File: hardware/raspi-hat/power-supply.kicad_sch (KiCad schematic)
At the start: 5 parts, among them J3 ATX-20, J4 Raspberry_Pi_4

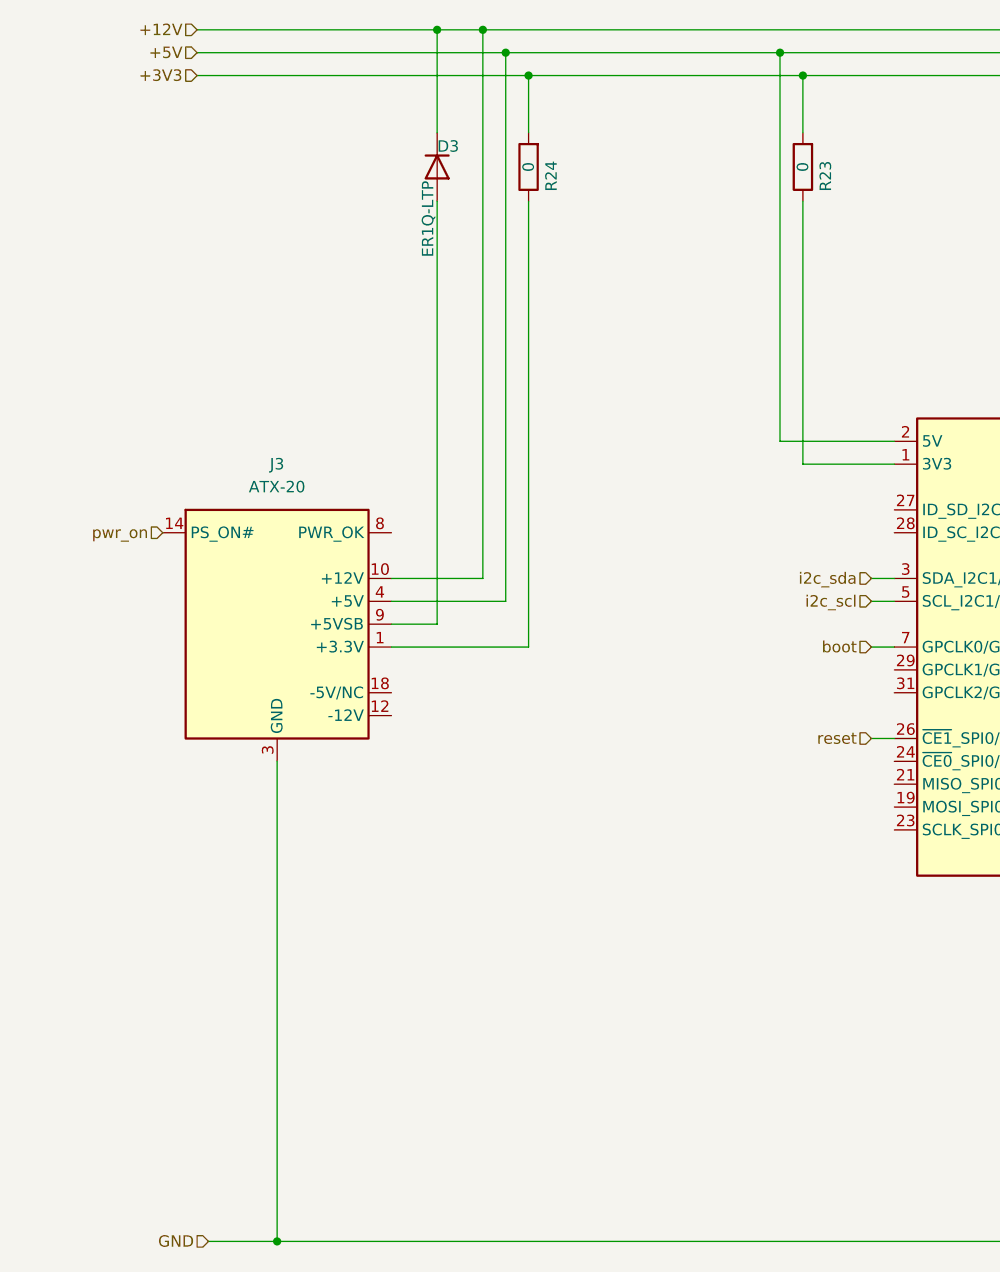
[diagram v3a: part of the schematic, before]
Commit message: added more parts
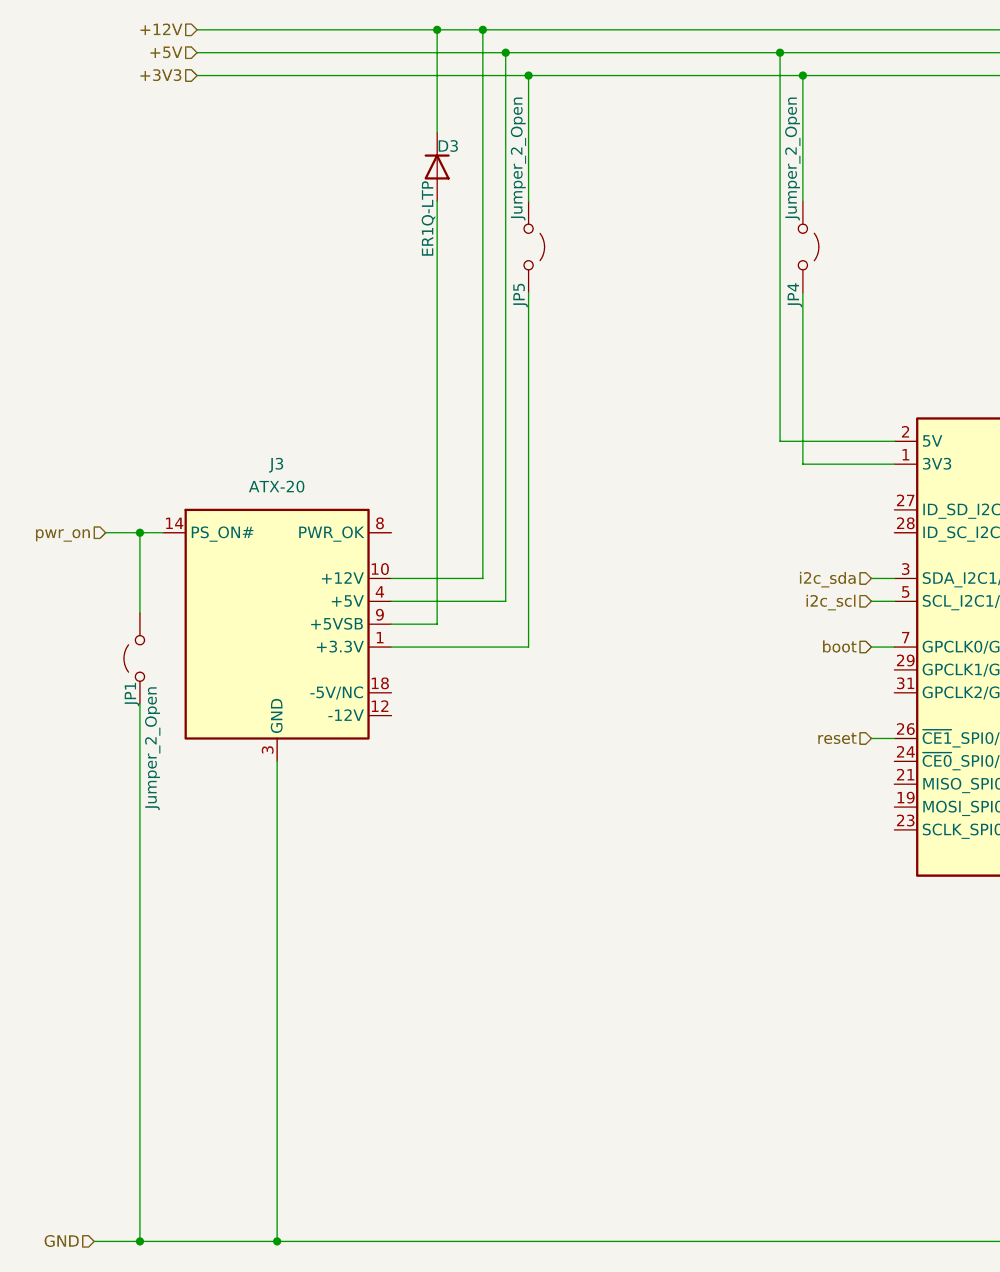
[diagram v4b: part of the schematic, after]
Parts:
- removed R23, R24: 0, Resistor_SMD:R_0603_1608Metric, symbol Device:R
- added JP1, JP4, JP5: Jumper_2_Open, Jumper:SolderJumper-2_P1.3mm_Open_TrianglePad1.0x1.5mm, symbol Jumper:Jumper_2_Open
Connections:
- net +3V3: now also JP4.1 (A), JP5.1 (A)
- net GND: now also JP1.1 (A)
- net pwr_on: now also JP1.2 (B)
- net at J3.1 (+3.3V), J3.11 (+3.3V), J3.2 (+3.3V): now also JP5.2 (B)
- net at J4.1 (3V3), J4.17 (3V3): now also JP4.2 (B)
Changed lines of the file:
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@@
+	)
+	(junction
+		(at 34.29 160.02)
+		(diameter 0)
+		(color 0 0 0 0)
 	)
 	(junction
@@
 	)
 	(junction
+		(at 34.29 81.28)
+		(diameter 0)
+		(color 0 0 0 0)
+	)
+	(junction
 		(at 151.13 160.02)
 		(diameter 0)
@@
 	(wire
 		(pts
-			(xy 107.95 30.48) (xy 107.95 36.83)
+			(xy 107.95 30.48) (xy 107.95 44.45)
 		)
 		(stroke
@@
 	(wire
 		(pts
+			(xy 34.29 81.28) (xy 36.83 81.28)
+		)
+		(stroke
+			(width 0)
+			(type default)
+		)
+	)
+	(wire
+		(pts
 			(xy 74.93 88.9) (xy 74.93 27.94)
 		)
@@
 	(wire
 		(pts
-			(xy 77.47 30.48) (xy 77.47 36.83)
+			(xy 77.47 30.48) (xy 77.47 44.45)
 		)
 		(stroke
@@
 	(wire
 		(pts
-			(xy 41.91 160.02) (xy 49.53 160.02)
-		)
-		(stroke
-			(width 0)
-			(type default)
-		)
-	)
-	(wire
-		(pts
-			(xy 77.47 44.45) (xy 77.47 93.98)
+			(xy 34.29 160.02) (xy 49.53 160.02)
+		)
+		(stroke
+			(width 0)
+			(type default)
+		)
+	)
+	(wire
+		(pts
+			(xy 29.21 160.02) (xy 34.29 160.02)
 		)
 		(stroke
@@
 	(wire
 		(pts
+			(xy 77.47 54.61) (xy 77.47 93.98)
+		)
+		(stroke
+			(width 0)
+			(type default)
+		)
+	)
+	(wire
+		(pts
 			(xy 40.64 25.4) (xy 67.31 25.4)
 		)
@@
 	(wire
 		(pts
-			(xy 107.95 44.45) (xy 107.95 73.66)
+			(xy 107.95 54.61) (xy 107.95 73.66)
 		)
 		(stroke
@@
 	(wire
 		(pts
+			(xy 34.29 100.33) (xy 34.29 160.02)
+		)
+		(stroke
+			(width 0)
+			(type default)
+		)
+	)
+	(wire
+		(pts
 			(xy 62.23 86.36) (xy 72.39 86.36)
 		)
@@
 	(wire
 		(pts
+			(xy 34.29 81.28) (xy 34.29 90.17)
+		)
+		(stroke
+			(width 0)
+			(type default)
+		)
+	)
+	(wire
+		(pts
 			(xy 49.53 160.02) (xy 151.13 160.02)
 		)
@@
 	(wire
 		(pts
+			(xy 30.48 81.28) (xy 34.29 81.28)
+		)
+		(stroke
+			(width 0)
+			(type default)
+		)
+	)
+	(wire
+		(pts
 			(xy 72.39 86.36) (xy 72.39 25.4)
 		)
@@
 	(hierarchical_label "pwr_on"
 		(shape input)
-		(at 36.83 81.28 180)
+		(at 30.48 81.28 180)
 		(effects
 			(font
@@
 	(hierarchical_label "GND"
 		(shape input)
-		(at 41.91 160.02 180)
+		(at 29.21 160.02 180)
 		(effects
 			(font
@@
 	)
 	(symbol
-		(lib_id "Device:R")
-		(at 77.47 40.64 180)
+		(lib_id "Jumper:Jumper_2_Open")
+		(at 34.29 95.25 90)
 		(unit 1)
 		(exclude_from_sim no)
@@
 		(on_board yes)
 		(dnp no)
-		(property "Reference" "R24"
-			(at 80.01 41.656 90)
-			(effects
-				(font
-					(size 1.27 1.27)
-				)
-			)
-		)
-		(property "Value" "0"
-			(at 77.47 40.64 90)
-			(effects
-				(font
-					(size 1.27 1.27)
-				)
-			)
-		)
-		(property "Footprint" "Resistor_SMD:R_0603_1608Metric"
-			(at 79.248 40.64 90)
+		(property "Reference" "JP1"
+			(at 33.274 97.79 0)
+			(effects
+				(font
+					(size 1.27 1.27)
+				)
+				(justify right)
+			)
+		)
+		(property "Value" "Jumper_2_Open"
+			(at 35.56 98.298 0)
+			(effects
+				(font
+					(size 1.27 1.27)
+				)
+				(justify right)
+			)
+		)
+		(property "Footprint" "Jumper:SolderJumper-2_P1.3mm_Open_TrianglePad1.0x1.5mm"
+			(at 34.29 95.25 0)
 			(effects
 				(font
@@
 		)
 		(property "Datasheet" "~"
-			(at 77.47 40.64 0)
-			(effects
-				(font
-					(size 1.27 1.27)
-				)
-				(hide yes)
-			)
-		)
-		(property "Description" "Resistor"
-			(at 77.47 40.64 0)
+			(at 34.29 95.25 0)
+			(effects
+				(font
+					(size 1.27 1.27)
+				)
+				(hide yes)
+			)
+		)
+		(property "Description" "Jumper, 2-pole, open"
+			(at 34.29 95.25 0)
+			(effects
+				(font
+					(size 1.27 1.27)
+				)
+				(hide yes)
+			)
+		)
+		(pin "2"
+		)
+		(pin "1"
+		)
+		(instances
+			(project ""
+				(path "/4679b2fb-3ee1-4560-bf60-3ee085e43370/c7d13d6e-bebd-45a0-80a7-7702da2d199e"
+					(reference "JP1")
+					(unit 1)
+				)
+			)
+		)
+	)
+	(symbol
+		(lib_id "Jumper:Jumper_2_Open")
+		(at 77.47 49.53 270)
+		(unit 1)
+		(exclude_from_sim no)
+		(in_bom yes)
+		(on_board yes)
+		(dnp no)
+		(property "Reference" "JP5"
+			(at 76.454 56.134 0)
+			(effects
+				(font
+					(size 1.27 1.27)
+				)
+				(justify right)
+			)
+		)
+		(property "Value" "Jumper_2_Open"
+			(at 76.2 46.482 0)
+			(effects
+				(font
+					(size 1.27 1.27)
+				)
+				(justify right)
+			)
+		)
+		(property "Footprint" "Jumper:SolderJumper-2_P1.3mm_Open_TrianglePad1.0x1.5mm"
+			(at 77.47 49.53 0)
+			(effects
+				(font
+					(size 1.27 1.27)
+				)
+				(hide yes)
+			)
+		)
+		(property "Datasheet" "~"
+			(at 77.47 49.53 0)
+			(effects
+				(font
+					(size 1.27 1.27)
+				)
+				(hide yes)
+			)
+		)
+		(property "Description" "Jumper, 2-pole, open"
+			(at 77.47 49.53 0)
 			(effects
 				(font
@@
 			(project "raspi-hat"
 				(path "/4679b2fb-3ee1-4560-bf60-3ee085e43370/c7d13d6e-bebd-45a0-80a7-7702da2d199e"
-					(reference "R24")
+					(reference "JP5")
+					(unit 1)
+				)
+			)
+		)
+	)
+	(symbol
+		(lib_id "Jumper:Jumper_2_Open")
+		(at 107.95 49.53 270)
+		(unit 1)
+		(exclude_from_sim no)
+		(in_bom yes)
+		(on_board yes)
+		(dnp no)
+		(property "Reference" "JP4"
+			(at 106.934 56.134 0)
+			(effects
+				(font
+					(size 1.27 1.27)
+				)
+				(justify right)
+			)
+		)
+		(property "Value" "Jumper_2_Open"
+			(at 106.68 46.482 0)
+			(effects
+				(font
+					(size 1.27 1.27)
+				)
+				(justify right)
+			)
+		)
+		(property "Footprint" "Jumper:SolderJumper-2_P1.3mm_Open_TrianglePad1.0x1.5mm"
+			(at 107.95 49.53 0)
+			(effects
+				(font
+					(size 1.27 1.27)
+				)
+				(hide yes)
+			)
+		)
+		(property "Datasheet" "~"
+			(at 107.95 49.53 0)
+			(effects
+				(font
+					(size 1.27 1.27)
+				)
+				(hide yes)
+			)
+		)
+		(property "Description" "Jumper, 2-pole, open"
+			(at 107.95 49.53 0)
+			(effects
+				(font
+					(size 1.27 1.27)
+				)
+				(hide yes)
+			)
+		)
+		(pin "2"
+		)
+		(pin "1"
+		)
+		(instances
+			(project "raspi-hat"
+				(path "/4679b2fb-3ee1-4560-bf60-3ee085e43370/c7d13d6e-bebd-45a0-80a7-7702da2d199e"
+					(reference "JP4")
 					(unit 1)
 				)
@@
 					(unit 1)
 				)
-			)
-		)
-	)
-	(symbol
-		(lib_id "Device:R")
-		(at 107.95 40.64 180)
-		(unit 1)
-		(exclude_from_sim no)
-		(in_bom yes)
-		(on_board yes)
-		(dnp no)
-		(property "Reference" "R23"
-			(at 110.49 41.656 90)
-			(effects
-				(font
-					(size 1.27 1.27)
-				)
-			)
-		)
-		(property "Value" "0"
-			(at 107.95 40.64 90)
-			(effects
-				(font
-					(size 1.27 1.27)
-				)
-			)
-		)
-		(property "Footprint" "Resistor_SMD:R_0603_1608Metric"
-			(at 109.728 40.64 90)
-			(effects
-				(font
-					(size 1.27 1.27)
-				)
-				(hide yes)
-			)
-		)
-		(property "Datasheet" "~"
-			(at 107.95 40.64 0)
-			(effects
-				(font
-					(size 1.27 1.27)
-				)
-				(hide yes)
-			)
-		)
-		(property "Description" "Resistor"
-			(at 107.95 40.64 0)
-			(effects
-				(font
-					(size 1.27 1.27)
-				)
-				(hide yes)
-			)
-		)
-		(pin "2"
-		)
-		(pin "1"
-		)
-		(instances
-			(project "raspi-hat"
-				(path "/4679b2fb-3ee1-4560-bf60-3ee085e43370/c7d13d6e-bebd-45a0-80a7-7702da2d199e"
-					(reference "R23")
-					(unit 1)
-				)

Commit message: updated hardware
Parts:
- added C12, C13, C14, C15, C16, C17: 1u, Capacitor_SMD:C_0603_1608Metric, symbol Device:C
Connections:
- net +12V: now also C12.1, C13.1, C14.1, C15.1, C16.1, C17.1
- net GND: now also C12.2, C13.2, C14.2, C15.2, C16.2, C17.2
